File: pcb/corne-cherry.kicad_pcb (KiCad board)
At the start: 2 copper layers, 275.5 x 105.6 mm, 124 parts, among them J1 Conn_01x03, J1 MJ-4PP-9, J2 OLED, J3 Conn_01x03, J3 MJ-4PP-9, J4 OLED, SW1 SW_PUSH, SW10 SW_PUSH, SW11 SW_PUSH, SW12 SW_PUSH, SW13 SW_PUSH, SW14 SW_PUSH, SW15 SW_PUSH, SW16 SW_PUSH, SW17 SW_PUSH, SW18 SW_PUSH, SW19 SW_PUSH, SW2 SW_PUSH, SW20 SW_PUSH, SW21 SW_PUSH, SW22 SW_PUSH, SW23 SW_PUSH, SW24 SW_PUSH, SW25 SW_PUSH, SW26 SW_PUSH, SW27 SW_PUSH, SW28 SW_PUSH, SW29 SW_PUSH, SW3 SW_PUSH, SW30 SW_PUSH, SW31 SW_PUSH, SW32 SW_PUSH, SW33 SW_PUSH, SW34 SW_PUSH, SW35 SW_PUSH, SW36 SW_PUSH, SW37 SW_PUSH, SW38 SW_PUSH, SW39 SW_PUSH, SW4 SW_PUSH, SW40 SW_PUSH, SW41 SW_PUSH, SW42 SW_PUSH, SW5 SW_PUSH, SW6 SW_PUSH, SW7 SW_PUSH, SW8 SW_PUSH, SW9 SW_PUSH, U1 ProMicro, U2 ProMicro

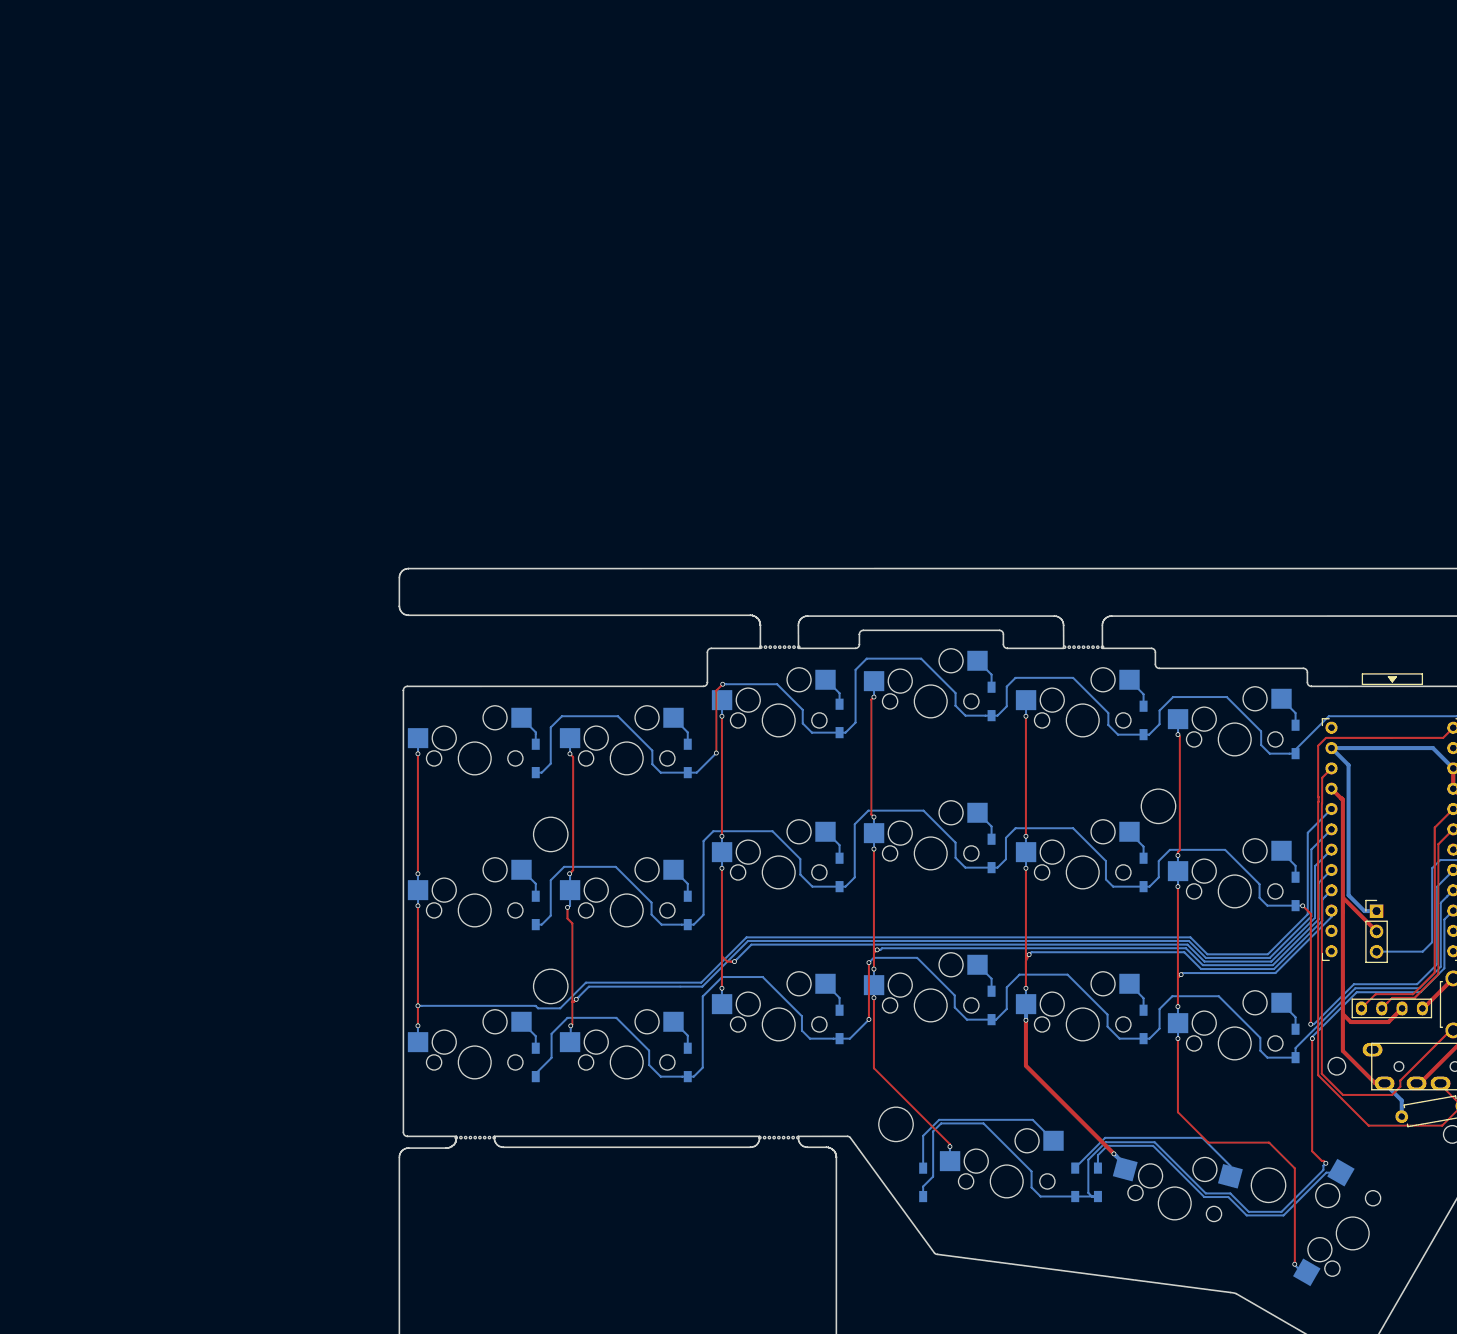
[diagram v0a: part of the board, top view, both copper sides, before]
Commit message: Begin RGB placing and routing
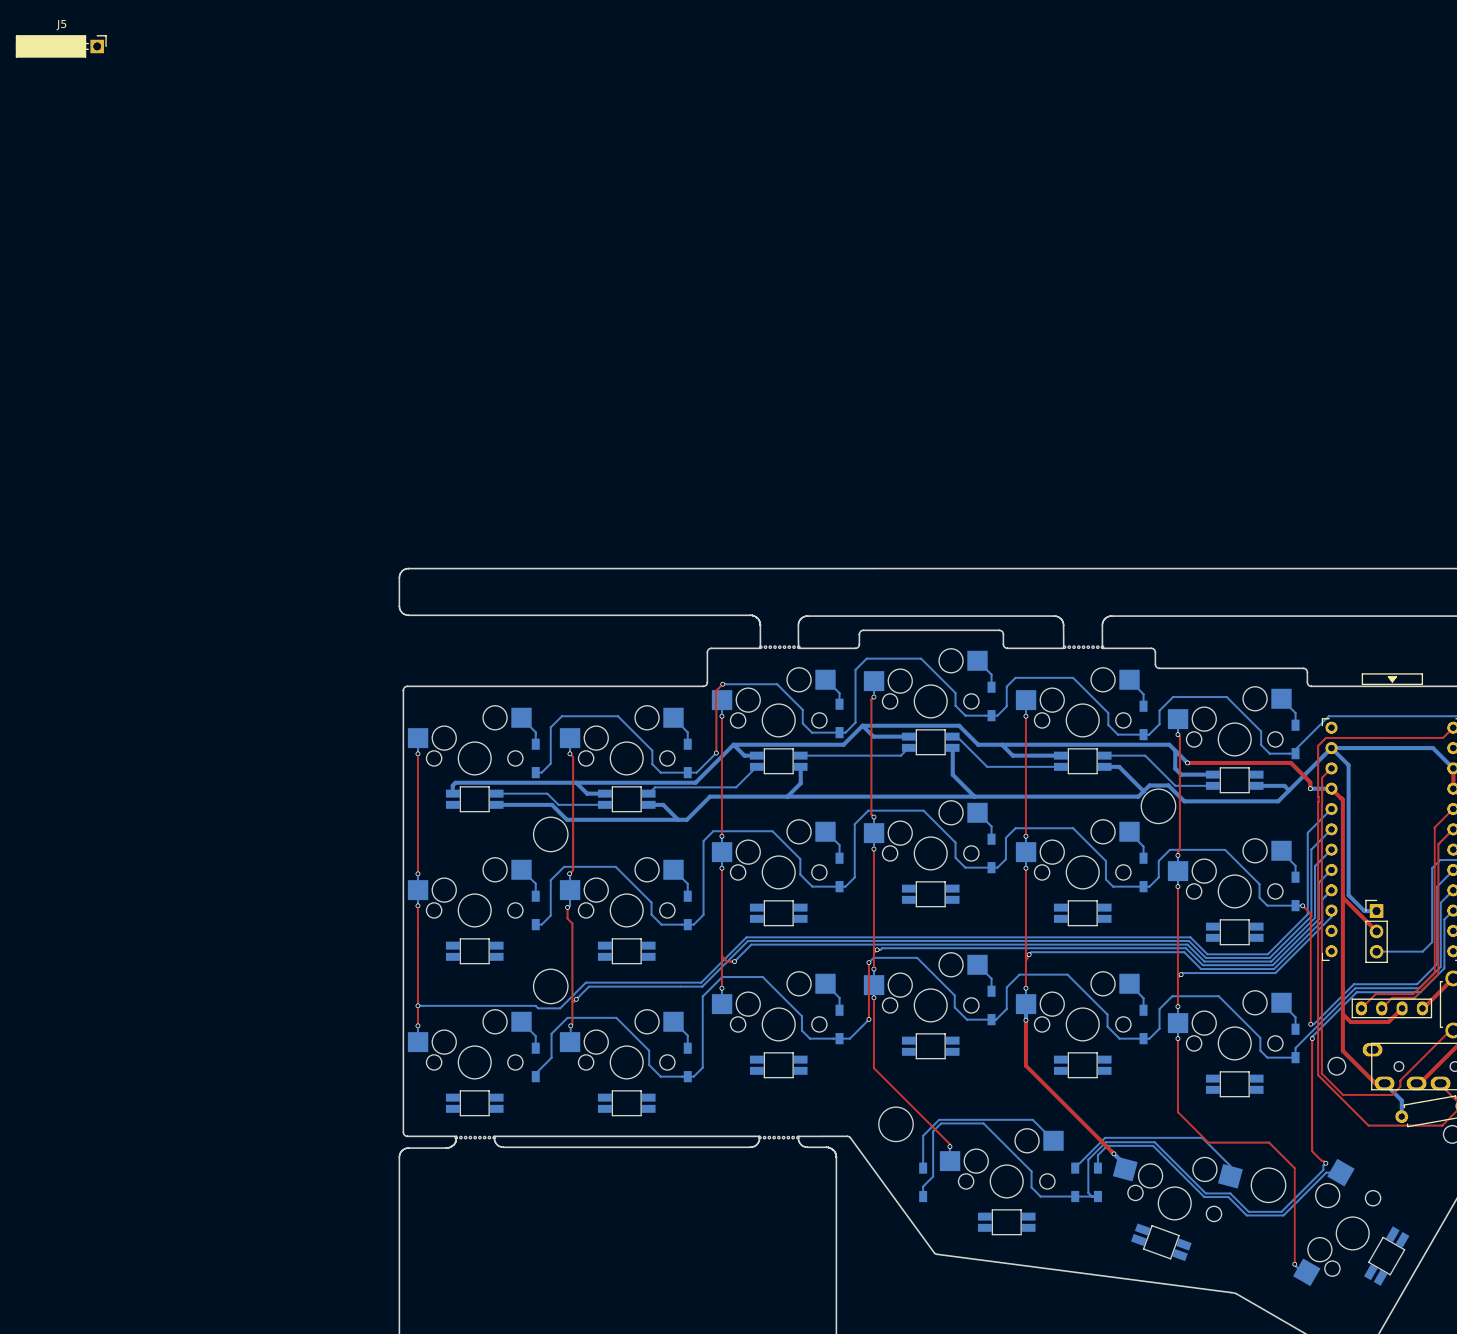
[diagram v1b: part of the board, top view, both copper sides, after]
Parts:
- added J5: Conn_01x01_Male, Connector_PinSocket_2.54mm:PinSocket_1x01_P2.54mm_Horizontal, F.Cu at (-27.1, -53.2)
- added LED1: YS-SK6812MINI-E, kbd:YS-SK6812MINI-E, B.Cu at (20.1, 40.9)
- added LED10: YS-SK6812MINI-E, kbd:YS-SK6812MINI-E, B.Cu at (77.1, 33.8)
- added LED11: YS-SK6812MINI-E, kbd:YS-SK6812MINI-E, B.Cu at (77.1, 52.8)
- added LED12: YS-SK6812MINI-E, kbd:YS-SK6812MINI-E, B.Cu at (77.1, 71.8)
- added LED13: YS-SK6812MINI-E, kbd:YS-SK6812MINI-E, B.Cu at (86.6, 93.8)
- added LED14: YS-SK6812MINI-E, kbd:YS-SK6812MINI-E, B.Cu at (96.1, 36.1)
- added LED15: YS-SK6812MINI-E, kbd:YS-SK6812MINI-E, B.Cu at (96.1, 55.1)
- added LED16: YS-SK6812MINI-E, kbd:YS-SK6812MINI-E, B.Cu at (96.1, 74.1)
- added LED17: YS-SK6812MINI-E, kbd:YS-SK6812MINI-E, B.Cu at (105.9, 96.3)
- added LED18: YS-SK6812MINI-E, kbd:YS-SK6812MINI-E, B.Cu at (115.1, 38.5)
- added LED19: YS-SK6812MINI-E, kbd:YS-SK6812MINI-E, B.Cu at (115.1, 57.5)
- added LED2: YS-SK6812MINI-E, kbd:YS-SK6812MINI-E, B.Cu at (20.1, 59.9)
- added LED20: YS-SK6812MINI-E, kbd:YS-SK6812MINI-E, B.Cu at (115.1, 76.5)
- added LED21: YS-SK6812MINI-E, kbd:YS-SK6812MINI-E, B.Cu at (134.1, 98.0)
- added LED3: YS-SK6812MINI-E, kbd:YS-SK6812MINI-E, B.Cu at (20.1, 78.9)
- added LED4: YS-SK6812MINI-E, kbd:YS-SK6812MINI-E, B.Cu at (39.1, 40.9)
- added LED5: YS-SK6812MINI-E, kbd:YS-SK6812MINI-E, B.Cu at (39.1, 59.9)
- added LED6: YS-SK6812MINI-E, kbd:YS-SK6812MINI-E, B.Cu at (39.1, 78.9)
- added LED7: YS-SK6812MINI-E, kbd:YS-SK6812MINI-E, B.Cu at (58.1, 36.1)
- added LED8: YS-SK6812MINI-E, kbd:YS-SK6812MINI-E, B.Cu at (58.1, 55.1)
- added LED9: YS-SK6812MINI-E, kbd:YS-SK6812MINI-E, B.Cu at (58.1, 74.1)
- renumbered J1 to P1, J3 to P3
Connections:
- P3 pad 2: VDD -> VCC
- SW1 pad 1: col0 -> Net-(SW1-Pad1)
- SW10 pad 1: col3 -> Net-(SW10-Pad1)
- SW11 pad 1: col4 -> Net-(SW11-Pad1)
- SW12 pad 1: col5 -> Net-(SW12-Pad1)
- SW16 pad 1: col3 -> Net-(SW16-Pad1)
- SW17 pad 1: col4 -> Net-(SW17-Pad1)
- SW18 pad 1: col5 -> Net-(SW18-Pad1)
- SW2 pad 1: col1 -> Net-(SW2-Pad1)
- SW22 pad 1: col0_r -> Net-(SW22-Pad1)
- SW23 pad 1: col1_r -> Net-(SW23-Pad1)
- SW24 pad 1: col2_r -> Net-(SW24-Pad1)
- SW25 pad 1: col3_r -> Net-(SW25-Pad1)
- SW26 pad 1: col4_r -> Net-(SW26-Pad1)
- SW27 pad 1: col5_r -> Net-(SW27-Pad1)
- SW28 pad 1: col0_r -> Net-(SW28-Pad1)
- SW29 pad 1: col1_r -> Net-(SW29-Pad1)
- SW3 pad 1: col2 -> Net-(SW3-Pad1)
- SW30 pad 1: col2_r -> Net-(SW30-Pad1)
- SW31 pad 1: col3_r -> Net-(SW31-Pad1)
- SW32 pad 1: col4_r -> Net-(SW32-Pad1)
- SW33 pad 1: col5_r -> Net-(SW33-Pad1)
- SW37 pad 1: col3_r -> Net-(SW37-Pad1)
- SW38 pad 1: col4_r -> Net-(SW38-Pad1)
- SW39 pad 1: col5_r -> Net-(SW39-Pad1)
- SW4 pad 1: col3 -> Net-(SW4-Pad1)
- SW5 pad 1: col4 -> Net-(SW5-Pad1)
- SW6 pad 1: col5 -> Net-(SW6-Pad1)
- SW7 pad 1: col0 -> Net-(SW7-Pad1)
- SW8 pad 1: col1 -> Net-(SW8-Pad1)
- SW9 pad 1: col2 -> Net-(SW9-Pad1)
- U1 pad 2: (no net) -> Net-(U1-Pad2)
- U2 pad 2: (no net) -> Net-(U2-Pad2)
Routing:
- net VCC: track 60.4 -> 207.1 mm, vias 0 -> 2
- net GND: track 90.2 -> 227.2 mm
- net Net-(LED14-Pad2): track 0.00 -> 15.1 mm
- net Net-(LED10-Pad2): track 0.00 -> 15.1 mm
- net Net-(LED4-Pad2): track 0.00 -> 14.9 mm
- net Net-(LED1-Pad2): track 0.00 -> 14.1 mm
- net Net-(LED10-Pad4): track 0.00 -> 13.9 mm

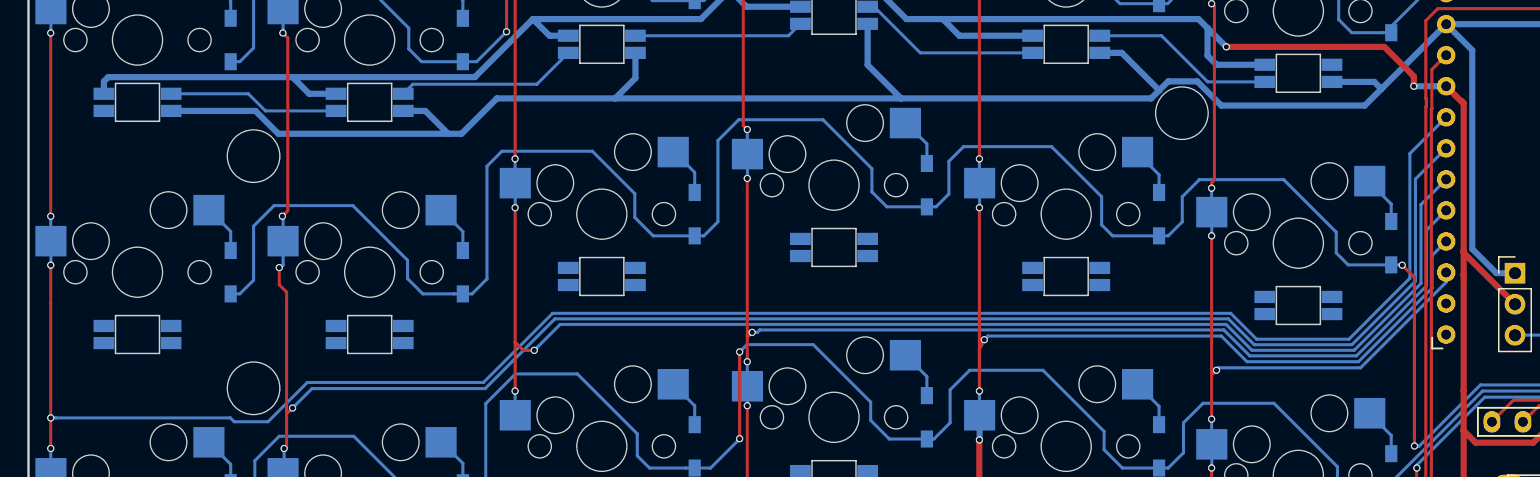
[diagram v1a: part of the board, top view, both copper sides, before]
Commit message: More rgb and fix G key
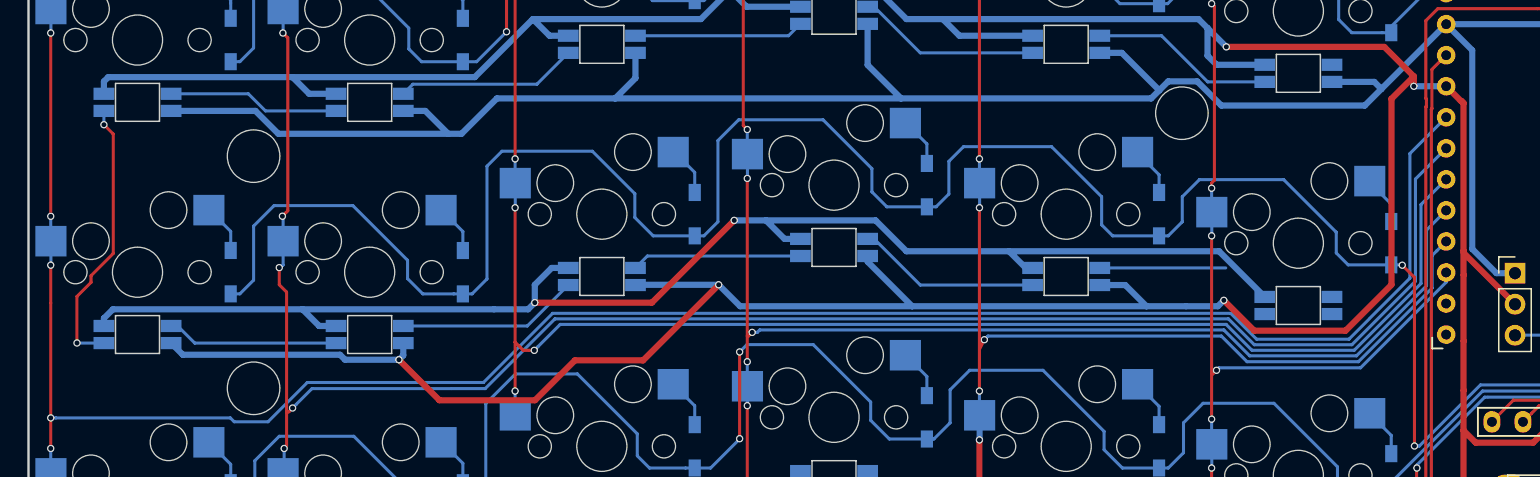
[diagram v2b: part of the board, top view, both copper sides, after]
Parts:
- turned LED11 to 180 degrees
- turned LED15 to 180 degrees
- turned LED19 to 180 degrees
- turned LED2 to 180 degrees
- turned LED5 to 180 degrees
- turned LED8 to 180 degrees
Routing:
- net VCC: track 207.1 -> 352.7 mm, vias 2 -> 5
- net GND: track 227.2 -> 342.8 mm, vias 0 -> 2
- net Net-(LED1-Pad4): track 0.00 -> 22.7 mm, vias 0 -> 2
- net Net-(LED11-Pad4): track 0.00 -> 15.1 mm
- net Net-(LED5-Pad4): track 0.00 -> 14.9 mm
- net Net-(LED2-Pad4): track 0.00 -> 14.1 mm
- net Net-(LED11-Pad2): track 0.00 -> 13.9 mm
- net Net-(LED15-Pad4): track 0.00 -> 10.8 mm

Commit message: Finish left half rgb
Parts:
- J5: footprint Connector_PinSocket_2.54mm:PinSocket_1x01_P2.54mm_Horizontal -> Connector_PinHeader_2.54mm:PinHeader_1x01_P2.54mm_Vertical
- moved J5 158.1 mm to (58.3, 79.8)
- turned LED13 to 180 degrees
- turned LED17 to 160 degrees
- turned LED21 to 240 degrees
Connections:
- LED20 pad 4: Net-(LED20-Pad4) -> Net-(LED16-Pad2)
- P3 pad 2: VCC -> VDD
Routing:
- net GND: track 342.8 -> 603.1 mm, vias 2 -> 4
- net VCC: track 352.7 -> 568.8 mm, vias 5 -> 7
- net Net-(J5-Pad1): track 0.00 -> 110.2 mm, vias 0 -> 1
- net Net-(LED13-Pad2): track 0.00 -> 74.2 mm
- net Net-(LED17-Pad4): track 0.00 -> 27.4 mm
- net Net-(LED19-Pad4): track 0.00 -> 24.7 mm, vias 0 -> 2
- net Net-(LED16-Pad2): track 0.00 -> 15.1 mm
- net Net-(LED12-Pad2): track 0.00 -> 15.1 mm
- net Net-(LED13-Pad4): track 0.00 -> 15.0 mm
- net Net-(LED6-Pad2): track 0.00 -> 14.9 mm
- net Net-(LED3-Pad2): track 0.00 -> 14.1 mm
- net Net-(LED12-Pad4): track 0.00 -> 13.9 mm
- net Net-(LED15-Pad4): track 10.8 -> 16.6 mm

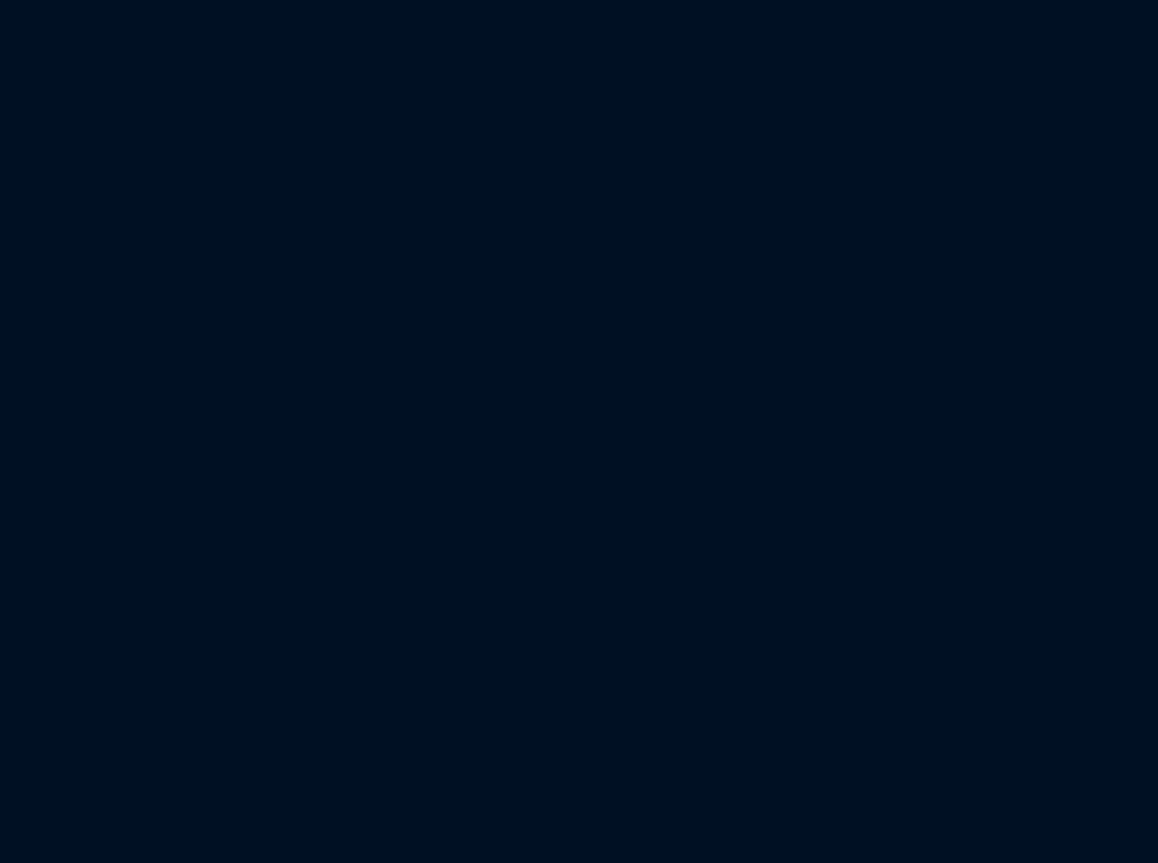
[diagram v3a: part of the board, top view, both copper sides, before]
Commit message: Add speakers and RGB on right half
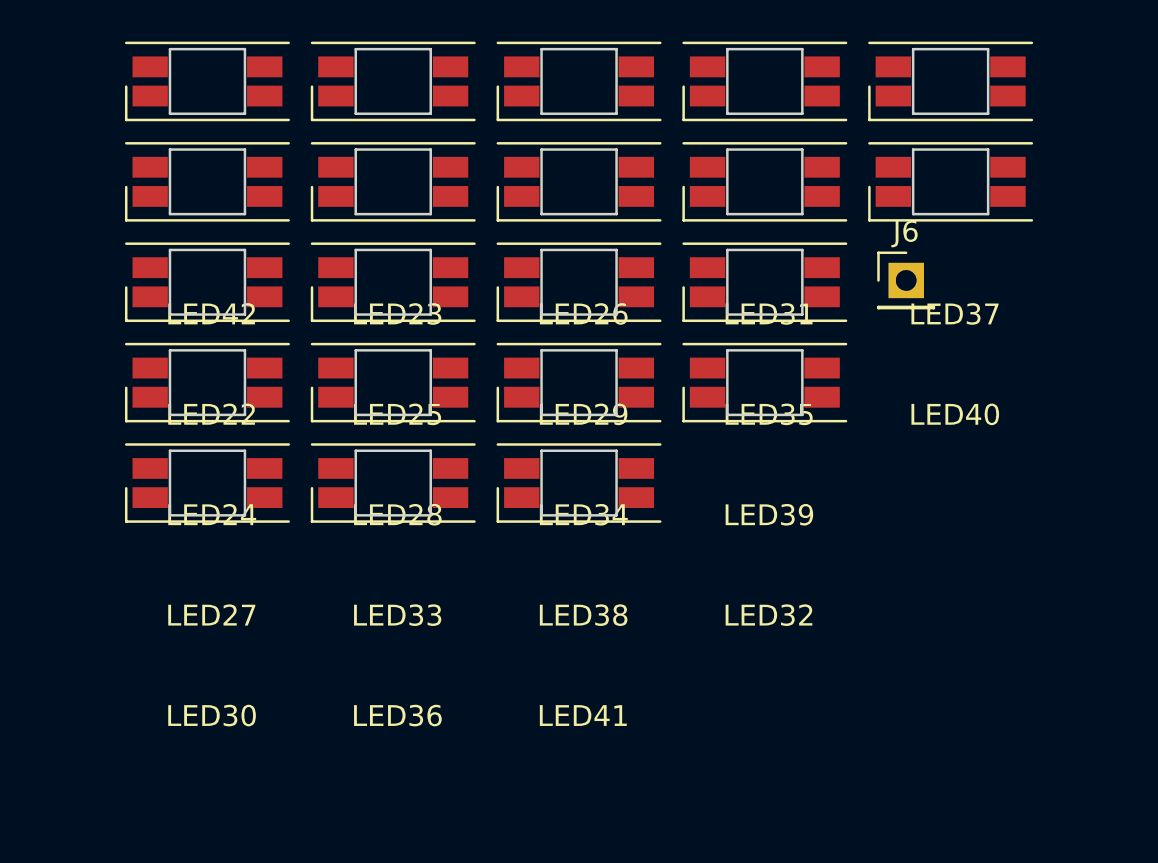
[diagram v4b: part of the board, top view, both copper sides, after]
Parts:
- added J6: Conn_01x01_Male, Connector_PinHeader_2.54mm:PinHeader_1x01_P2.54mm_Vertical, F.Cu at (202.3, -17.9)
- added LED22: YS-SK6812MINI-E, kbd:YS-SK6812MINI-E, F.Cu at (168.7, -22.6)
- added LED23: YS-SK6812MINI-E, kbd:YS-SK6812MINI-E, F.Cu at (177.7, -27.4)
- added LED24: YS-SK6812MINI-E, kbd:YS-SK6812MINI-E, F.Cu at (168.7, -17.8)
- added LED25: YS-SK6812MINI-E, kbd:YS-SK6812MINI-E, F.Cu at (177.7, -22.6)
- added LED26: YS-SK6812MINI-E, kbd:YS-SK6812MINI-E, F.Cu at (186.6, -27.4)
- added LED27: YS-SK6812MINI-E, kbd:YS-SK6812MINI-E, F.Cu at (168.7, -12.9)
- added LED28: YS-SK6812MINI-E, kbd:YS-SK6812MINI-E, F.Cu at (177.7, -17.8)
- added LED29: YS-SK6812MINI-E, kbd:YS-SK6812MINI-E, F.Cu at (186.6, -22.6)
- added LED30: YS-SK6812MINI-E, kbd:YS-SK6812MINI-E, F.Cu at (168.7, -8.13)
- added LED31: YS-SK6812MINI-E, kbd:YS-SK6812MINI-E, F.Cu at (195.5, -27.4)
- added LED32: YS-SK6812MINI-E, kbd:YS-SK6812MINI-E, F.Cu at (195.5, -12.9)
- added LED33: YS-SK6812MINI-E, kbd:YS-SK6812MINI-E, F.Cu at (177.7, -12.9)
- added LED34: YS-SK6812MINI-E, kbd:YS-SK6812MINI-E, F.Cu at (186.6, -17.8)
- added LED35: YS-SK6812MINI-E, kbd:YS-SK6812MINI-E, F.Cu at (195.5, -22.6)
- added LED36: YS-SK6812MINI-E, kbd:YS-SK6812MINI-E, F.Cu at (177.7, -8.13)
- added LED37: YS-SK6812MINI-E, kbd:YS-SK6812MINI-E, F.Cu at (204.4, -27.4)
- added LED38: YS-SK6812MINI-E, kbd:YS-SK6812MINI-E, F.Cu at (186.6, -12.9)
- added LED39: YS-SK6812MINI-E, kbd:YS-SK6812MINI-E, F.Cu at (195.5, -17.8)
- added LED40: YS-SK6812MINI-E, kbd:YS-SK6812MINI-E, F.Cu at (204.4, -22.6)
- added LED41: YS-SK6812MINI-E, kbd:YS-SK6812MINI-E, F.Cu at (186.6, -8.13)
- added LED42: YS-SK6812MINI-E, kbd:YS-SK6812MINI-E, F.Cu at (168.7, -27.4)
